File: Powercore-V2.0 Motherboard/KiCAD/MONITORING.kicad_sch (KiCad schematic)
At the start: 6 parts, among them Q6 DMG2302UK-7

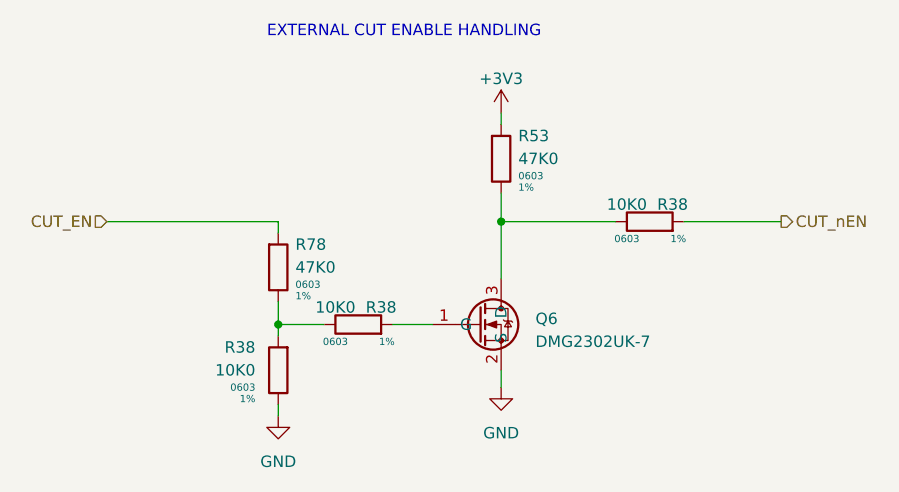
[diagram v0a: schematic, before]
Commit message: Attempt to mitigate failure mode
Replaced gate driver
Replaced FETs
Added input filter to gate driver
Removed input PI filter
Updated control timing to reduce initial metastability
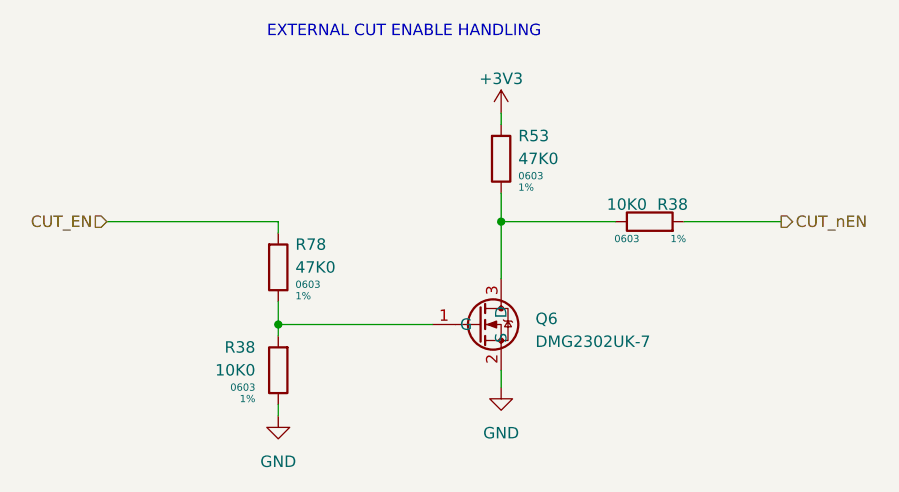
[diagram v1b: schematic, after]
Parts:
- removed R38: 10K0, Resistor_SMD:R_0603_1608Metric, symbol 0603_RES:10K0
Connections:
- net at Q6.1 (G): now also R38.1, R78.2
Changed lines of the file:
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@@
     (stroke (width 0) (type default))
   )
-  (wire (pts (xy 149.86 100.33) (xy 145.415 100.33))
+  (wire (pts (xy 132.715 100.33) (xy 149.86 100.33))
     (stroke (width 0) (type default))
   )
@@
   )
   (wire (pts (xy 157.48 88.9) (xy 170.18 88.9))
-    (stroke (width 0) (type default))
-  )
-  (wire (pts (xy 137.795 100.33) (xy 132.715 100.33))
     (stroke (width 0) (type default))
   )
@@
         )
       )
-    )
-  )
-  (symbol (lib_id "0603_RES:10K0") (at 141.605 100.33 270) (mirror x) (unit 1)
-    (in_bom yes) (on_board yes) (dnp no)
-    (property "Reference" "R38" (at 144.145 98.425 90)
-      (effects (font (size 1.27 1.27)))
-    )
-    (property "Value" "10K0" (at 139.065 98.425 90)
-      (effects (font (size 1.27 1.27)))
-    )
-    (property "Footprint" "Resistor_SMD:R_0603_1608Metric" (at 120.015 109.22 0)
-      (effects (font (size 1.27 1.27)) hide)
-    )
-    (property "Datasheet" "https://www.seielect.com/Catalog/SEI-RMCF_RMCP.pdf" (at 122.555 97.79 0)
-      (effects (font (size 1.27 1.27)) hide)
-    )
-    (property "Package Size" "0603" (at 139.065 102.235 90)
-      (effects (font (size 0.8 0.8) (color 0 72 72 1)))
-    )
-    (property "Tolerance" "1%" (at 144.78 102.235 90)
-      (effects (font (size 0.8 0.8) (color 0 72 72 1)))
-    )
-    (property "Part Number" "RMCF0603FT10K0" (at 123.825 110.49 0)
-      (effects (font (size 1.27 1.27)) hide)
-    )
-    (property "Manufacturer" "Stackpole" (at 141.605 100.33 0)
-      (effects (font (size 1.27 1.27)) hide)
-    )
-    (pin "1")
-    (pin "2")
-    (instances
-      (project "POWERCORE-V2.0_MOTHERBOARD"
-        (path "/f573d926-a852-4f5d-b1ba-3c18778d48e1/b27e7b44-e012-4854-958f-f20bfe477dbb"
-          (reference "R38") (unit 1)
-        )
-        (path "/f573d926-a852-4f5d-b1ba-3c18778d48e1/299f7a06-bdb8-4c3b-9ee6-50f605303c57"
-          (reference "R80") (unit 1)
-        )
-      )
